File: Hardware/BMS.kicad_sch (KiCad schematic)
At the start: 12 parts, among them IC1 STM32H742VIT6

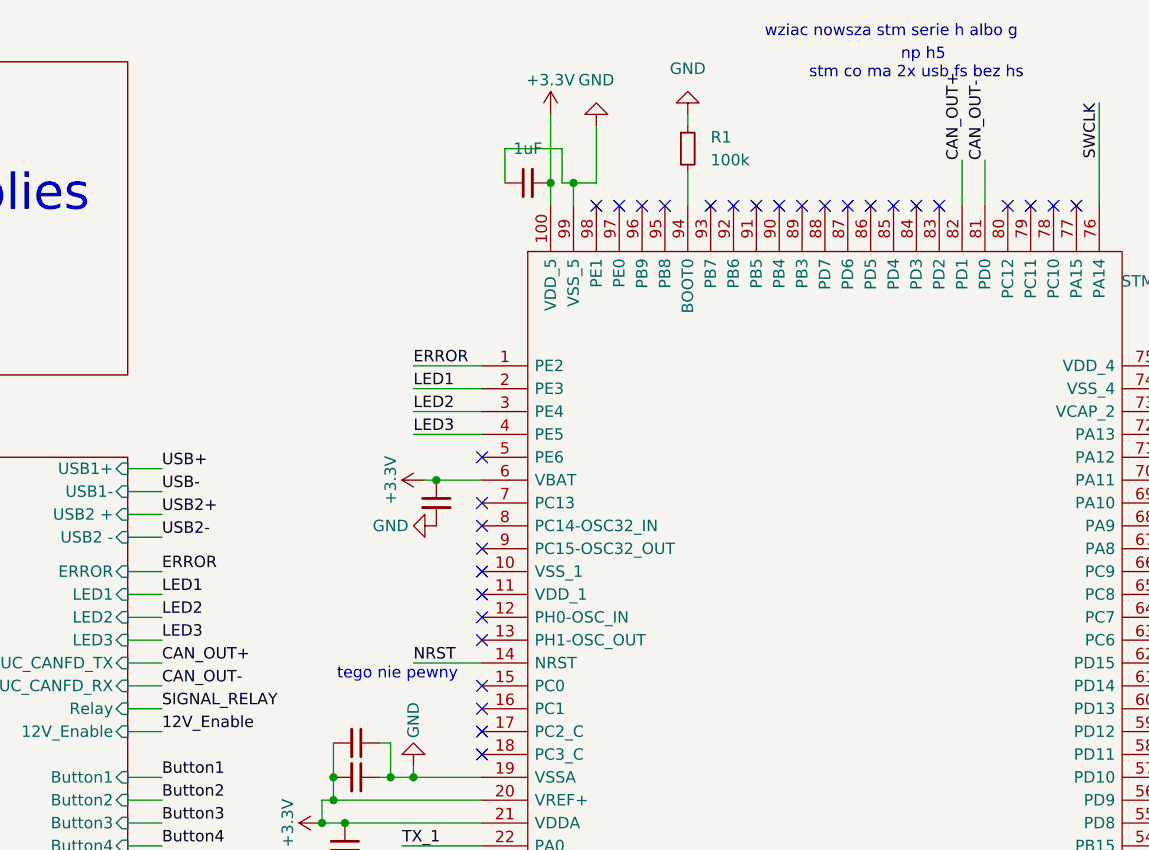
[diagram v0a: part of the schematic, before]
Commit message: Dodano wyjaśnienia w schemacie, zmieniono nazewnictwo wewnętrzne lini can
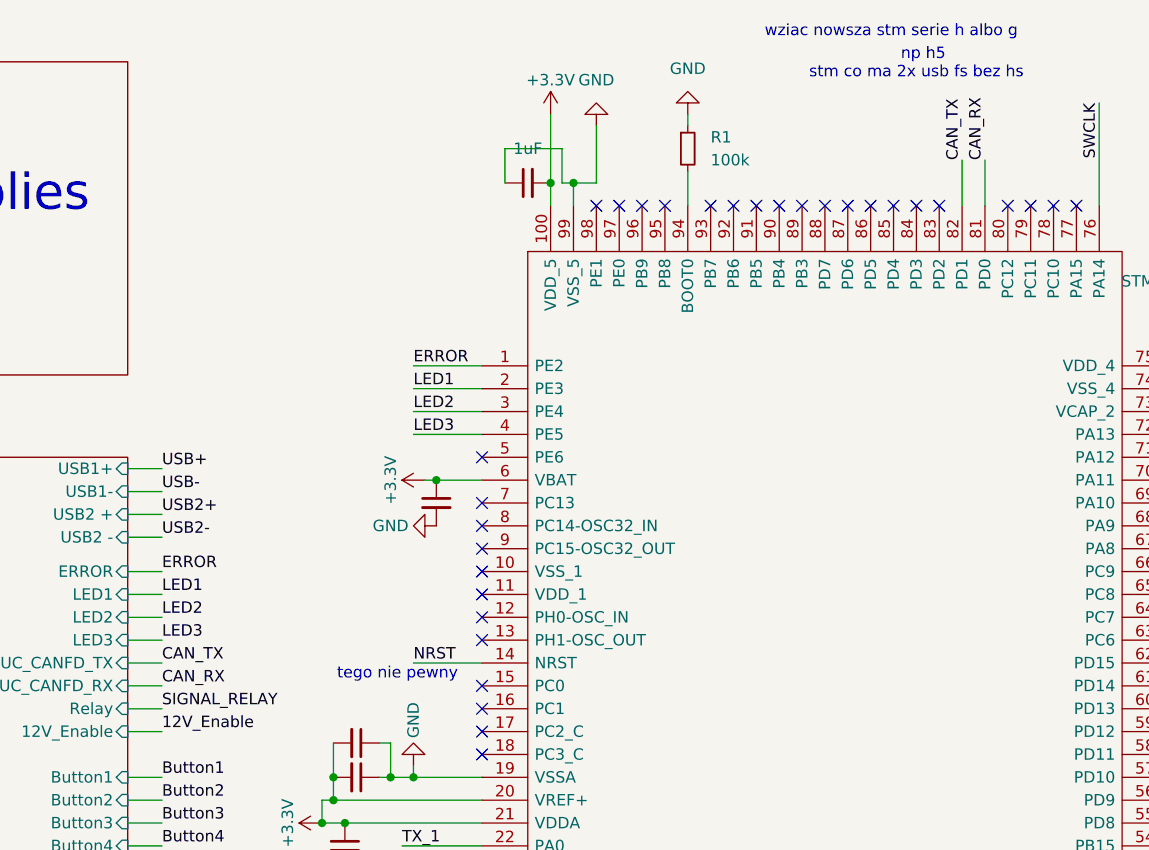
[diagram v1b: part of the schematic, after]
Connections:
- net CAN_OUT+ renamed CAN_TX
- net CAN_OUT- renamed CAN_RX
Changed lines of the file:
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@@
-		)
-	)
-	(label "CAN_OUT+"
-		(at 83.82 87.63 0)
-		(effects
-			(font
-				(size 1.27 1.27)
-			)
-			(justify left bottom)
 		)
 	)
@@
 		)
 	)
-	(label "CAN_OUT+"
+	(label "CAN_TX"
 		(at 172.72 31.75 90)
 		(effects
@@
 		)
 	)
-	(label "CAN_OUT-"
-		(at 83.82 90.17 0)
-		(effects
-			(font
-				(size 1.27 1.27)
-			)
-			(justify left bottom)
-		)
-	)
 	(label "USB2+"
 		(at 83.82 71.12 0)
@@
 		)
 	)
+	(label "CAN_RX"
+		(at 83.82 90.17 0)
+		(effects
+			(font
+				(size 1.27 1.27)
+			)
+			(justify left bottom)
+		)
+	)
 	(label "12V_Enable"
 		(at 134.62 148.59 90)
@@
 		)
 	)
-	(label "CAN_OUT-"
+	(label "CAN_RX"
 		(at 175.26 31.75 90)
 		(effects
@@
 		(effects
 			(font
+				(size 1.27 1.27)
+			)
+			(justify left bottom)
+		)
+	)
+	(label "CAN_TX"
+		(at 83.82 87.63 0)
+		(effects
+			(font

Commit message: zmiany w kodzier bq
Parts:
- added H1, H2, H3, H4: MountingHole, MountingHole:MountingHole_2.2mm_M2_Pad_Via, symbol Mechanical:MountingHole

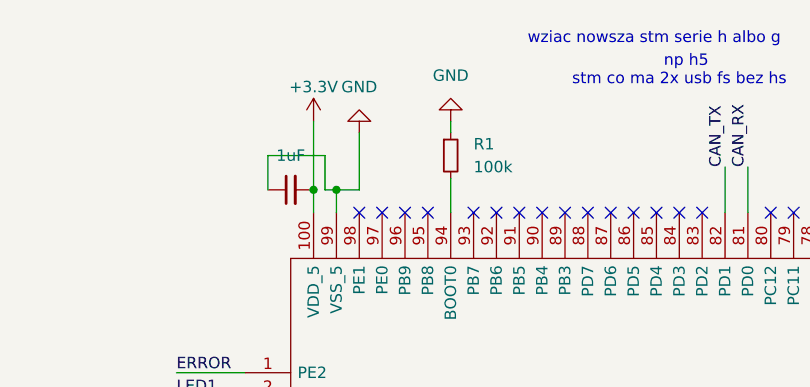
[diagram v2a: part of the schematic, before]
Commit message: Dodano logikę ładowania bateri, zabezpieczenia OV UV na przekaźniku działają poprawnie, przekaźnik ma swój test polegający na styku pomocniczym
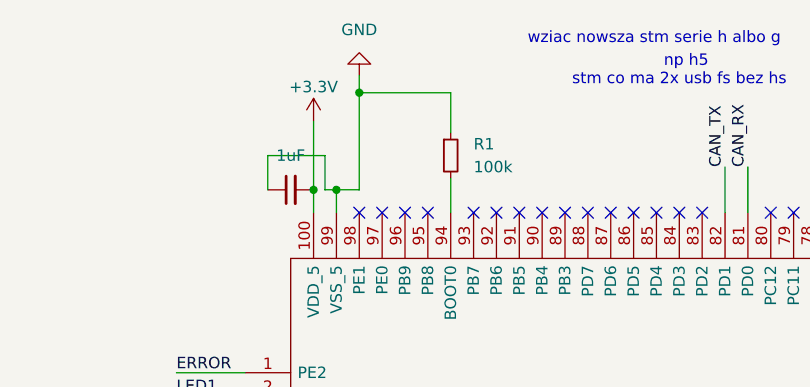
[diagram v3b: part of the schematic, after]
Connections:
- net GND: now also R1.1
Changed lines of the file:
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@@
+	)
+	(junction
+		(at 132.08 23.495)
+		(diameter 0)
+		(color 0 0 0 0)
 	)
 	(junction
@@
 	(wire
 		(pts
+			(xy 132.08 23.495) (xy 132.08 34.29)
+		)
+		(stroke
+			(width 0)
+			(type default)
+		)
+	)
+	(wire
+		(pts
 			(xy 80.01 68.58) (xy 83.82 68.58)
 		)
@@
 	(wire
 		(pts
-			(xy 132.08 27.94) (xy 132.08 34.29)
+			(xy 132.08 21.59) (xy 132.08 23.495)
 		)
 		(stroke
@@
 	(wire
 		(pts
-			(xy 142.24 26.67) (xy 142.24 27.94)
+			(xy 142.24 23.495) (xy 142.24 27.94)
 		)
 		(stroke
@@
 		(pts
 			(xy 228.6 27.94) (xy 219.71 27.94)
+		)
+		(stroke
+			(width 0)
+			(type default)
+		)
+	)
+	(wire
+		(pts
+			(xy 142.24 23.495) (xy 132.08 23.495)
 		)
 		(stroke
@@
 				(path "/26289bb6-56bc-4ca1-b1a2-18d58d1afdf5"
 					(reference "#PWR010")
-					(unit 1)
-				)
-			)
-		)
-	)
-	(symbol
-		(lib_name "GND_2")
-		(lib_id "power:GND")
-		(at 142.24 26.67 180)
-		(unit 1)
-		(exclude_from_sim no)
-		(in_bom yes)
-		(on_board yes)
-		(dnp no)
-		(fields_autoplaced yes)
-		(property "Reference" "#PWR08"
-			(at 142.24 20.32 0)
-			(effects
-				(font
-					(size 1.27 1.27)
-				)
-				(hide yes)
-			)
-		)
-		(property "Value" "GND"
-			(at 142.24 21.59 0)
-			(effects
-				(font
-					(size 1.27 1.27)
-				)
-			)
-		)
-		(property "Footprint" ""
-			(at 142.24 26.67 0)
-			(effects
-				(font
-					(size 1.27 1.27)
-				)
-				(hide yes)
-			)
-		)
-		(property "Datasheet" ""
-			(at 142.24 26.67 0)
-			(effects
-				(font
-					(size 1.27 1.27)
-				)
-				(hide yes)
-			)
-		)
-		(property "Description" "Power symbol creates a global label with name \"GND\" , ground"
-			(at 142.24 26.67 0)
-			(effects
-				(font
-					(size 1.27 1.27)
-				)
-				(hide yes)
-			)
-		)
-		(pin "1"
-		)
-		(instances
-			(project "BMS"
-				(path "/26289bb6-56bc-4ca1-b1a2-18d58d1afdf5"
-					(reference "#PWR08")
 					(unit 1)
 				)
@@
 	(symbol
 		(lib_id "power:GND")
-		(at 132.08 27.94 180)
+		(at 132.08 21.59 180)
 		(unit 1)
 		(exclude_from_sim no)
@@
 		(fields_autoplaced yes)
 		(property "Reference" "#PWR06"
+			(at 132.08 15.24 0)
+			(effects
+				(font
+					(size 1.27 1.27)
+				)
+				(hide yes)
+			)
+		)
+		(property "Value" "GND"
+			(at 132.08 16.51 0)
+			(effects
+				(font
+					(size 1.27 1.27)
+				)
+			)
+		)
+		(property "Footprint" ""
 			(at 132.08 21.59 0)
 			(effects
@@
 			)
 		)
-		(property "Value" "GND"
-			(at 132.08 22.86 0)
-			(effects
-				(font
-					(size 1.27 1.27)
-				)
-			)
-		)
-		(property "Footprint" ""
-			(at 132.08 27.94 0)
-			(effects
-				(font
-					(size 1.27 1.27)
-				)
-				(hide yes)
-			)
-		)
 		(property "Datasheet" ""
-			(at 132.08 27.94 0)
+			(at 132.08 21.59 0)
 			(effects
 				(font
@@
 		)
 		(property "Description" "Power symbol creates a global label with name \"GND\" , ground"
-			(at 132.08 27.94 0)
-			(effects
-				(font
+			(at 132.08 21.59 0)
+			(effects
+				(font

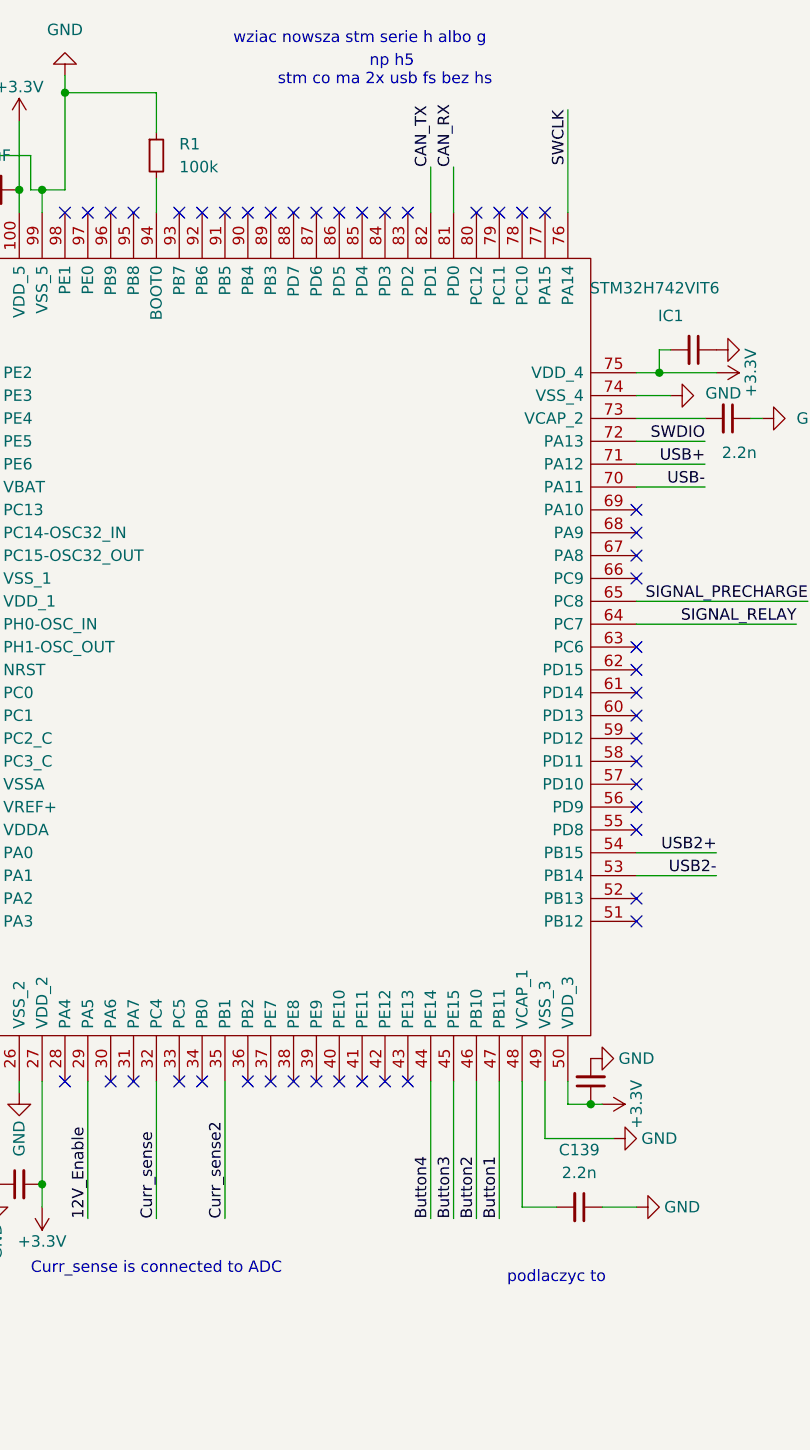
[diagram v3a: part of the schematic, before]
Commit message: Zmiany wizualne w schemacie
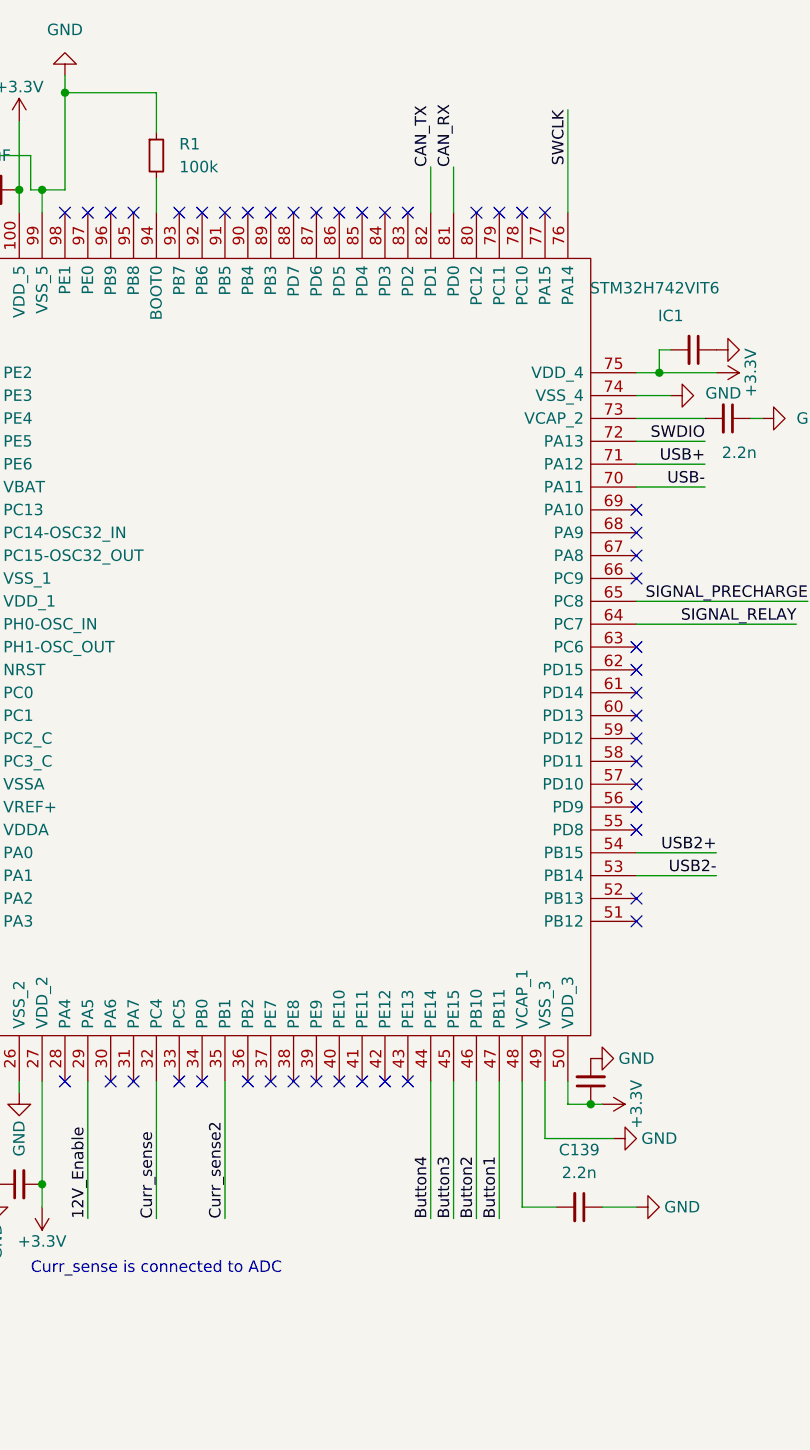
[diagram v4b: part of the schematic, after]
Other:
- note removed: "np h5"
- note removed: "podlaczyc to"
- note removed: "stm co ma 2x usb fs bez hs"
- note removed: "wziac nowsza stm serie h albo g"
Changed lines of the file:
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@@
-		)
-	)
-	(text "podlaczyc to\n"
-		(exclude_from_sim no)
-		(at 186.69 155.194 0)
-		(effects
-			(font
-				(size 1.27 1.27)
-			)
 		)
 	)
@@
 		)
 	)
-	(text "np h5"
-		(exclude_from_sim no)
-		(at 168.402 20.066 0)
-		(effects
-			(font
-				(size 1.27 1.27)
-			)
-		)
-	)
-	(text "wziac nowsza stm serie h albo g"
-		(exclude_from_sim no)
-		(at 164.846 17.526 0)
-		(effects
-			(font
-				(size 1.27 1.27)
-			)
-		)
-	)
 	(text "Curr_sense is connected to ADC "
 		(exclude_from_sim no)
@@
 		(effects
 			(font
-				(size 1.27 1.27)
-			)
-		)
-	)
-	(text "stm co ma 2x usb fs bez hs"
-		(exclude_from_sim no)
-		(at 167.64 22.098 0)
-		(effects
-			(font
